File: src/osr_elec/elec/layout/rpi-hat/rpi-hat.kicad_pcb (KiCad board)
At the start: 4 copper layers, 65 x 56.5 mm, 76 parts

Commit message: refactor: can termination switch from ck-js-series package
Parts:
- R10: value 100mW Thick Film Resistors 75V ±100ppm/℃ ±1% 402Ω 0603 Chip Resistor - Surface Mount ROHS -> 100mW Thick Film Resistors ±100ppm/℃ ±1% 402Ω 0603 Chip Resistor - Surface Mount ROHS
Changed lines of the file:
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@@
 			)
 		)
-		(property "Value" "100mW Thick Film Resistors 75V ±100ppm/℃ ±1% 402Ω 0603  Chip Resistor - Surface Mount ROHS"
+		(property "Value" "100mW Thick Film Resistors ±100ppm/℃ ±1% 402Ω 0603  Chip Resistor - Surface Mount ROHS"
 			(at 0 1.43 90)
 			(layer "F.Fab")
@@
 		)
 		(group ""
-			(members "5491bdfd-be93-4776-a4e2-2ded867d77dc" "865cfbd7-3afb-4ad8-a3b9-51c185d3dd04")
-		)
-		(model "${KIPRJMOD}/../../footprints/footprints.3dshapes/CK_JS102011JCQN_SW_SPDT_Slide_SMD.step"
+			(members "63f66163-6e17-4d3a-927d-62f3a41a09c1" "76a51ac0-f8fc-45e7-89f3-8a54b5269056")
+		)
+		(model "${KIPRJMOD}/../../../build/footprints/footprints.3dshapes/CK_JS102011JCQN_SW_SPDT_Slide_SMD.step"
 			(offset
 				(xyz 0 -1.8 -0)

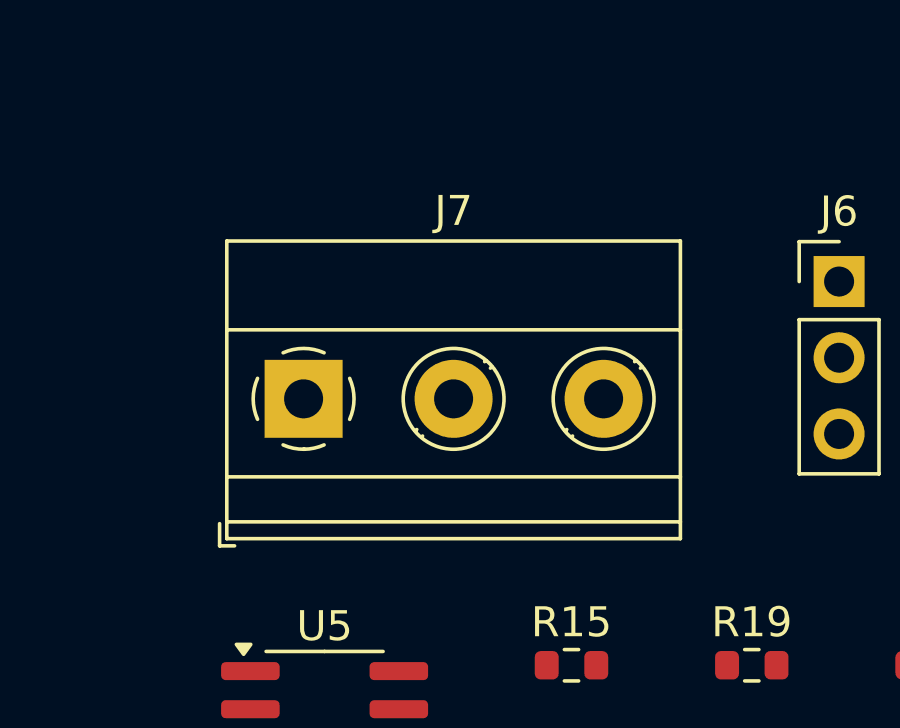
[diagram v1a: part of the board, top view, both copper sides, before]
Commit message: refactor: terminal block from package phoenix-pt-series
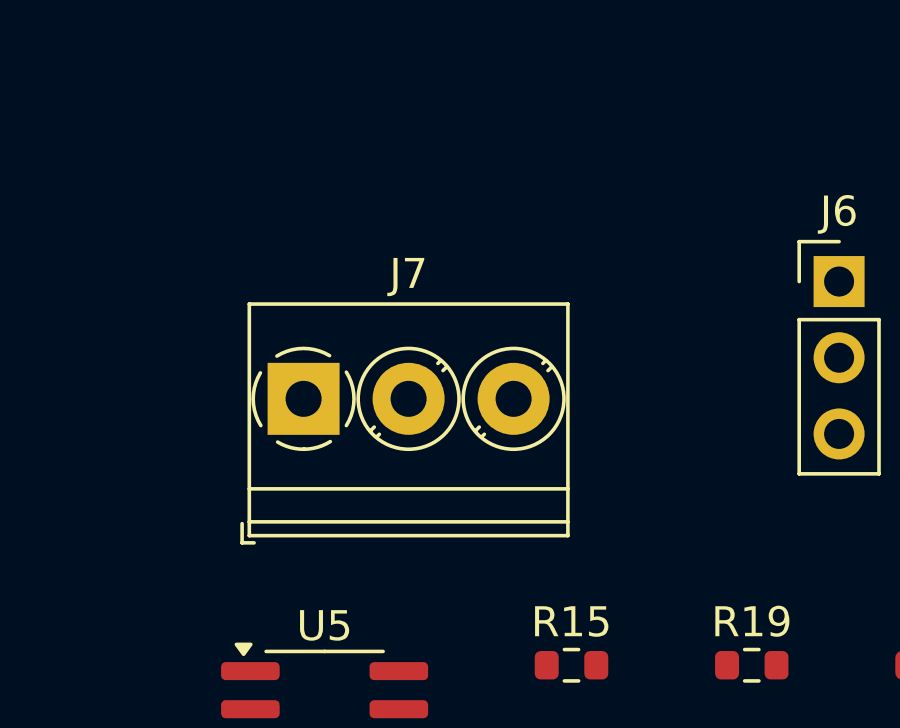
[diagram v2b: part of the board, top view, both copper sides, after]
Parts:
- J7: footprint lib:TerminalBlock_Phoenix_MKDS-1,5-3_1x03_P5.00mm_Horizontal -> lib:TerminalBlock_Phoenix_PT-1,5-3-3.5-H_1x03_P3.50mm_Horizontal

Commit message: refactor: use kicad global libs for terminal block
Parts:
- J7: footprint lib:TerminalBlock_Phoenix_PT-1,5-3-3.5-H_1x03_P3.50mm_Horizontal -> TerminalBlock_Phoenix:TerminalBlock_Phoenix_PT-1,5-3-3.5-H_1x03_P3.50mm_Horizontal
- R10: value 100mW Thick Film Resistors ±100ppm/℃ ±1% 402Ω 0603 Chip Resistor - Surface Mount ROHS -> 100mW Thick Film Resistors 75V ±100ppm/℃ ±1% 402Ω 0603 Chip Resistor - Surface Mount ROHS
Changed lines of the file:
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@@
 			)
 		)
-		(property "Value" "100mW Thick Film Resistors ±100ppm/℃ ±1% 402Ω 0603  Chip Resistor - Surface Mount ROHS"
+		(property "Value" "100mW Thick Film Resistors 75V ±100ppm/℃ ±1% 402Ω 0603  Chip Resistor - Surface Mount ROHS"
 			(at 0 1.43 90)
 			(layer "F.Fab")
@@
 		)
 	)
-	(footprint "lib:TerminalBlock_Phoenix_PT-1,5-3-3.5-H_1x03_P3.50mm_Horizontal"
+	(footprint "TerminalBlock_Phoenix:TerminalBlock_Phoenix_PT-1,5-3-3.5-H_1x03_P3.50mm_Horizontal"
 		(layer "F.Cu")
 		(at 52.075 90.535)
@@
 			)
 		)
-		(property "Footprint" "lib:TerminalBlock_Phoenix_MKDS-1,5-3_1x03_P5.00mm_Horizontal"
+		(property "Footprint" "TerminalBlock_Phoenix:TerminalBlock_Phoenix_PT-1,5-3-3.5-H_1x03_P3.50mm_Horizontal"
 			(at 0 0 0)
 			(unlocked yes)
@@
 			(pintype "stereo")
 		)
-		(model "${KIPRJMOD}/../../../build/footprints/footprints.3dshapes/TerminalBlock_Phoenix_PT-1,5-3-3.5-H_1x03_P3.50mm_Horizontal.wrl"
+		(model "${KICAD8_3DMODEL_DIR}/TerminalBlock_Phoenix.3dshapes/TerminalBlock_Phoenix_PT-1,5-3-3.5-H_1x03_P3.50mm_Horizontal.wrl"
 			(offset
 				(xyz 0 0 0)
